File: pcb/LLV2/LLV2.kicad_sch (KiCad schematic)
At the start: 1 part, among them U1 XIAO-nRF52840-SMD

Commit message: Begin drafting final PCB layout
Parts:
- added J1: Conn_01x02, Connector_PinHeader_2.54mm:PinHeader_1x02_P2.54mm_Vertical_SMD_Pin1Right, symbol Connector_Generic:Conn_01x02
- added U2: MAX30102, OptoDevice:Maxim_OLGA-14_3.3x5.6mm_P0.8mm, symbol Sensor:MAX30102
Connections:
- net +3V3: now reaches U1.12 (3V3_OUT)
- net +3V3: now also U2.11 (VDD)
- net GND: now reaches U1.13 (GND)
- net GND: now also U1.18 (GND), U1.20 (GND), J1.2 (Pin_2), U2.12 (GND)
- net at U1.19 (VBAT): now also J1.1 (Pin_1)
- net at U1.5 (D4): now also U2.3 (SDA)
- net at U1.6 (D5): now also U2.2 (SCL)
- new net: U2.10 (VLED+), U2.9 (VLED+)

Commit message: PCBV2 updates
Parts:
- added BZ1: Buzzer, Package_SO:SOIC-8_3.9x4.9mm_P1.27mm, symbol Device:Buzzer
- added SW1: SW_Push, Package_SO:SOIC-8_3.9x4.9mm_P1.27mm, symbol Switch:SW_Push
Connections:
- net GND: now also SW1.1
- net at U1.4 (D3): now also SW1.2

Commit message: PCBV2 updates 10/12
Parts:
- added D1, D2: 1N4148W, Diode_SMD:D_SOD-123, symbol Diode:1N4148W
- added M1: Motor_DC, symbol Motor:Motor_DC
- added Q1, Q2: AO3400A, Package_TO_SOT_SMD:SOT-23, symbol Transistor_FET:AO3400A
- added R1, R3: 1K, Resistor_SMD:R_0603_1608Metric, symbol Device:R
- added R2, R4: 100K, Resistor_SMD:R_0603_1608Metric, symbol Device:R
- U2: footprint OptoDevice:Maxim_OLGA-14_3.3x5.6mm_P0.8mm -> MAX30102SMD:MAX30102_SMD
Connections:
- net +3V3: now also BZ1.1 (+), D1.1 (K), D2.1 (K), M1.1 (+)
- net GND: now also Q1.2 (S), Q2.2 (S), R2.2, R4.2
- net at BZ1.2 (-): now also D2.2 (A), Q2.3 (D)
- net at U1.2 (D1): now also R3.1
- net at U1.3 (D2): now also R1.2
- new net: Q2.1 (G), R3.2, R4.1
- new net: Q1.1 (G), R1.1, R2.1
- new net: D1.2 (A), M1.2 (-), Q1.3 (D)
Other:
- moved on the sheet: BZ1

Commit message: PCBV2 edits
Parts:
- SW1: footprint Package_SO:SOIC-8_3.9x4.9mm_P1.27mm -> easyeda2kicad:KEY-SMD_4P-L4.8-W4.6-P1.70-LS6.2
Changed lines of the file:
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@@
 			)
 		)
-		(property "Footprint" "Package_SO:SOIC-8_3.9x4.9mm_P1.27mm"
+		(property "Footprint" "easyeda2kicad:KEY-SMD_4P-L4.8-W4.6-P1.70-LS6.2"
 			(at 96.52 80.01 0)
 			(hide yes)

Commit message: PCBV2 updates 10/20
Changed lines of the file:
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@@
 	(wire
 		(pts
-			(xy 76.2 85.09) (xy 91.44 85.09)
+			(xy 87.63 85.09) (xy 91.44 85.09)
 		)
 		(stroke
@@
 	(symbol
 		(lib_id "power:GND")
-		(at 76.2 85.09 270)
+		(at 87.63 85.09 270)
 		(unit 1)
 		(body_style 1)
@@
 		(fields_autoplaced yes)
 		(property "Reference" "#PWR08"
-			(at 69.85 85.09 0)
+			(at 81.28 85.09 0)
 			(hide yes)
 			(show_name no)
@@
 		)
 		(property "Value" "GND"
-			(at 72.39 85.0899 90)
+			(at 83.82 85.0899 90)
 			(show_name no)
 			(do_not_autoplace no)
@@
 		)
 		(property "Footprint" ""
-			(at 76.2 85.09 0)
+			(at 87.63 85.09 0)
 			(hide yes)
 			(show_name no)
@@
 		)
 		(property "Datasheet" ""
-			(at 76.2 85.09 0)
+			(at 87.63 85.09 0)
 			(hide yes)
 			(show_name no)
@@
 		)
 		(property "Description" "Power symbol creates a global label with name \"GND\" , ground"
-			(at 76.2 85.09 0)
-			(hide yes)
-			(show_name no)
+			(at 87.63 85.09 0)
+			(hide yes)
+			(show_name no)

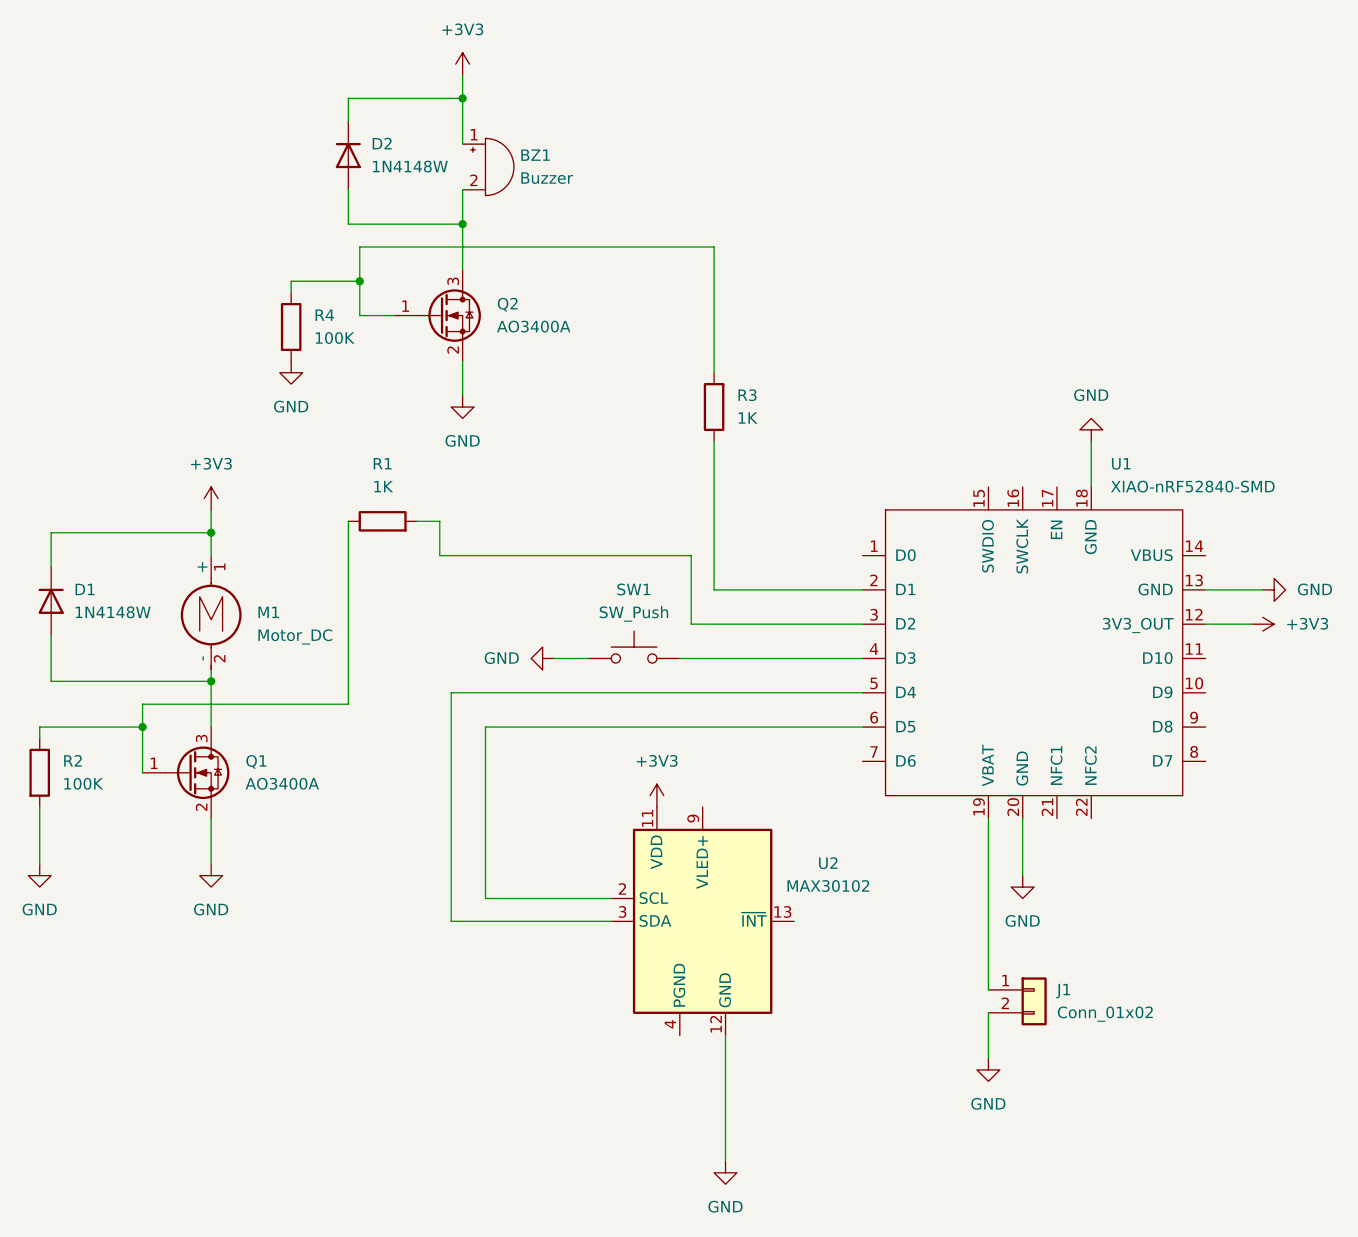
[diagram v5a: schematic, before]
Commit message: Major PCBV2 edits + Fall Detection Overhaul
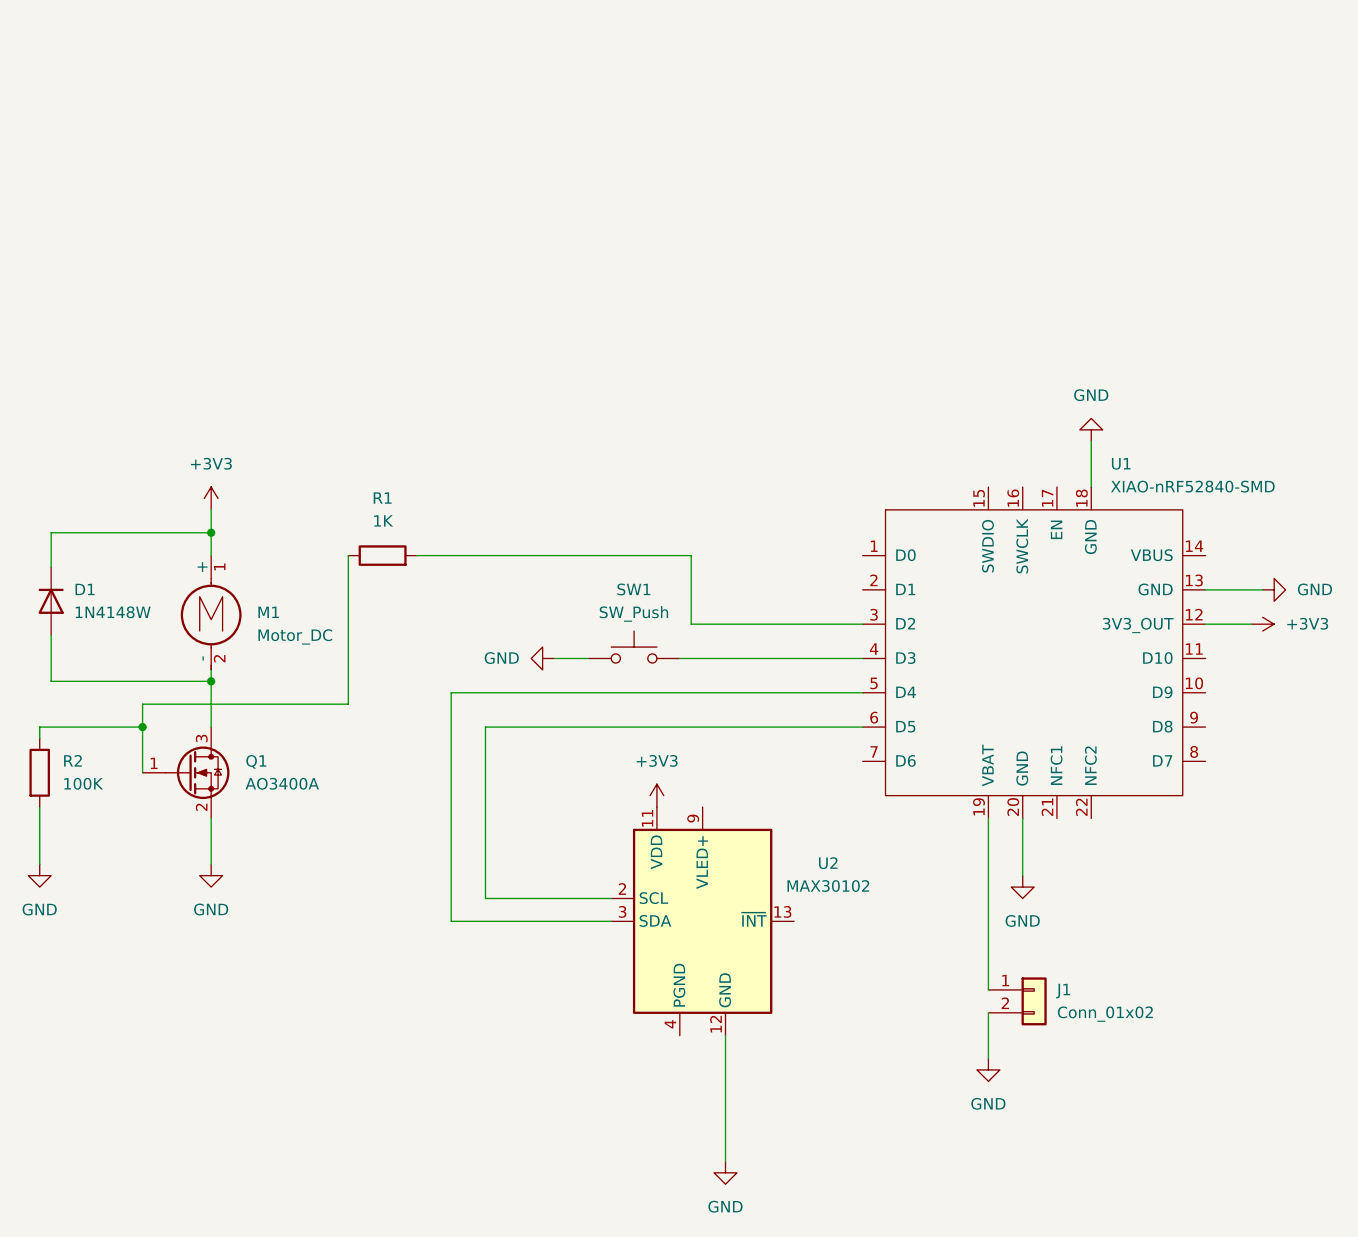
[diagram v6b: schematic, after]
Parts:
- removed BZ1: Buzzer, Package_SO:SOIC-8_3.9x4.9mm_P1.27mm, symbol Device:Buzzer
- removed D2: 1N4148W, Diode_SMD:D_SOD-123, symbol Diode:1N4148W
- removed Q2: AO3400A, Package_TO_SOT_SMD:SOT-23, symbol Transistor_FET:AO3400A
- removed R3: 1K, Resistor_SMD:R_0603_1608Metric, symbol Device:R
- removed R4: 100K, Resistor_SMD:R_0603_1608Metric, symbol Device:R
- J1: footprint Connector_PinHeader_2.54mm:PinHeader_1x02_P2.54mm_Vertical_SMD_Pin1Right -> CustomSolderPads:Battery_Copper_Pads
- M1: footprint (none) -> CustomSolderPads:Battery_Copper_Pads
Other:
- moved on the sheet: R1

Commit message: PCBV2 updates 10/27
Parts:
- D1: footprint Diode_SMD:D_SOD-123 -> Diode_SMD:D_SOD-323
- R1, R2: footprint Resistor_SMD:R_0603_1608Metric -> Resistor_SMD:R_0402_1005Metric
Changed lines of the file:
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@@
 			)
 		)
-		(property "Footprint" "Resistor_SMD:R_0603_1608Metric"
+		(property "Footprint" "Resistor_SMD:R_0402_1005Metric"
 			(at 68.58 75.438 90)
 			(hide yes)
@@
 			)
 		)
-		(property "Footprint" "Resistor_SMD:R_0603_1608Metric"
+		(property "Footprint" "Resistor_SMD:R_0402_1005Metric"
 			(at 28.702 97.79 90)
 			(hide yes)
@@
 			)
 		)
-		(property "Footprint" "Diode_SMD:D_SOD-123"
+		(property "Footprint" "Diode_SMD:D_SOD-323"
 			(at 27.305 78.74 0)
 			(hide yes)
